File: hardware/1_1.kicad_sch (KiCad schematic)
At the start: 38 parts, among them U1 CH32V203C8U6, U10 SN74LVC1G32DBVR, U2 ZD24C02B-MAGMT, U3 32.768kHz, U5 SD101CWS, U7 HX_JN1_27-2X5P_ZZ_H4_9, U9 SN74LVC1G32DBVR, X1 8MHz

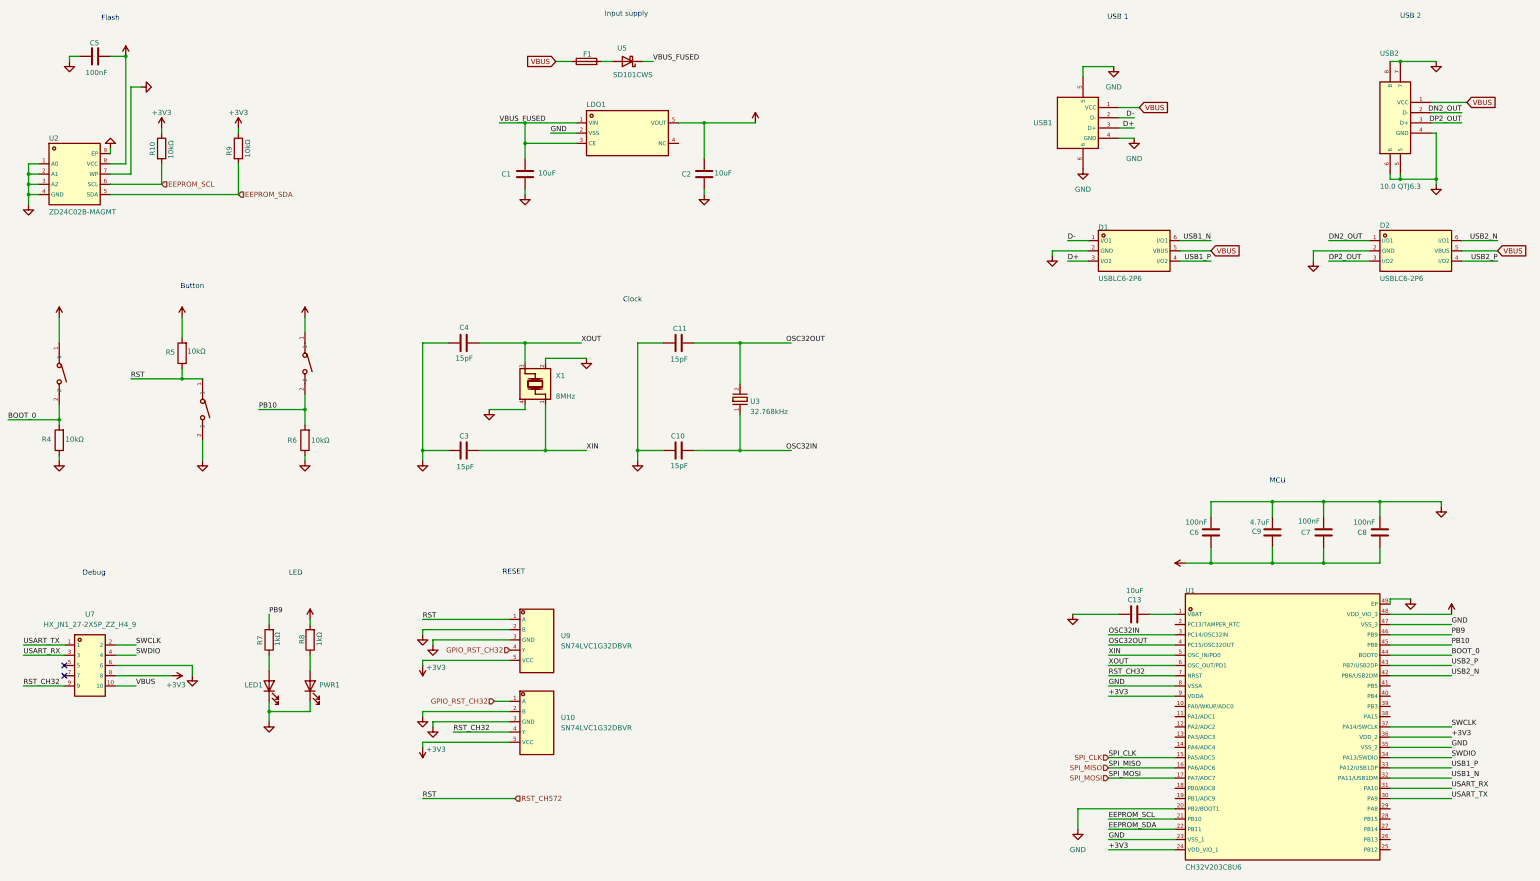
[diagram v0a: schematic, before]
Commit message: refactor: minor schematic visual changes
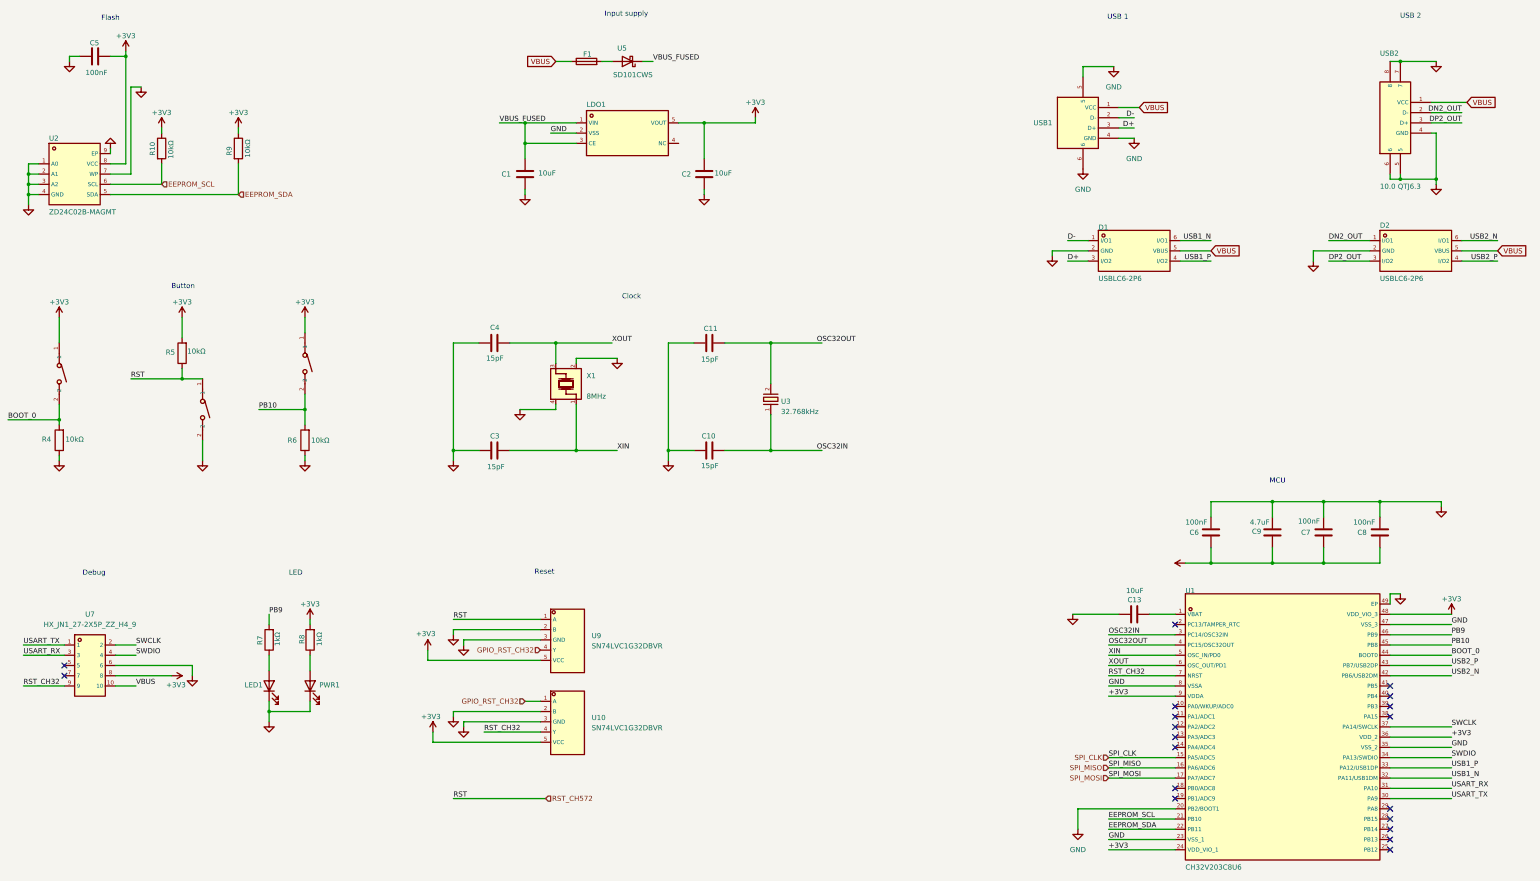
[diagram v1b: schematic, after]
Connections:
- no-connect marks 2 -> 19
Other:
- note added: "Reset"
- note removed: "RESET"
- moved on the sheet: C10, C11, C3, C4, U10, U3, U9, X1

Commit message: fix: add missing cs line to spi bus
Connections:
- net SPI_CS: now reaches U1.14 (PA4/ADC4)
- no-connect marks 19 -> 18
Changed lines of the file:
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@@
-	)
-	(no_connect
-		(at 311.15 205.74)
 	)
 	(no_connect
@@
 	(wire
 		(pts
+			(xy 294.64 205.74) (xy 311.15 205.74)
+		)
+		(stroke
+			(width 0)
+			(type default)
+		)
+	)
+	(wire
+		(pts
 			(xy 284.48 80.01) (xy 289.56 80.01)
 		)
@@
 			)
 			(justify right bottom)
+		)
+	)
+	(label "SPI_CS"
+		(at 294.64 205.74 0)
+		(effects
+			(font
+				(size 1.27 1.27)
+			)
+			(justify left bottom)
 		)
 	)
@@
 		(effects
 			(font
+				(size 1.27 1.27)
+			)
+			(justify right)
+		)
+	)
+	(hierarchical_label "SPI_CS"
+		(shape input)
+		(at 294.64 205.74 180)
+		(effects
+			(font

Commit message: add developemnt board and fix issue related to dual i2c access
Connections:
- net GPIO_I2C_CTRL: now reaches U1.18 (PB0/ADC8)
- net GPIO_RESERVED_1: now reaches U1.19 (PB1/ADC9)
- no-connect marks 18 -> 16
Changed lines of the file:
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@@
-	)
-	(no_connect
-		(at 311.15 218.44)
 	)
 	(no_connect
@@
 	)
 	(no_connect
-		(at 311.15 215.9)
-	)
-	(no_connect
 		(at 311.15 175.26)
 	)
@@
 	(wire
 		(pts
+			(xy 294.64 215.9) (xy 311.15 215.9)
+		)
+		(stroke
+			(width 0)
+			(type default)
+		)
+	)
+	(wire
+		(pts
 			(xy 320.04 80.01) (xy 312.42 80.01)
 		)
@@
 		(pts
 			(xy 162.56 120.65) (xy 162.56 132.08)
+		)
+		(stroke
+			(width 0)
+			(type default)
+		)
+	)
+	(wire
+		(pts
+			(xy 294.64 218.44) (xy 311.15 218.44)
 		)
 		(stroke
@@
 		)
 	)
+	(hierarchical_label "GPIO_I2C_CTRL"
+		(shape input)
+		(at 294.64 215.9 180)
+		(effects
+			(font
+				(size 1.27 1.27)
+			)
+			(justify right)
+		)
+	)
 	(hierarchical_label "GPIO_RST_CH32"
 		(shape input)
@@
 		)
 	)
+	(hierarchical_label "GPIO_RESERVED_1"
+		(shape input)
+		(at 294.64 218.44 180)
+		(effects
+			(font
+				(size 1.27 1.27)
+			)
+			(justify right)
+		)
+	)
